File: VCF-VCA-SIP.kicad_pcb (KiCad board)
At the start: 2 copper layers, 46 x 18 mm, 45 parts, among them P1 CONN_10, Q1 BC857BS, U1 LM13700, U2 TL072-, U3 LM13700, U4 TL072-, U5 LM13700, U6 TL072-

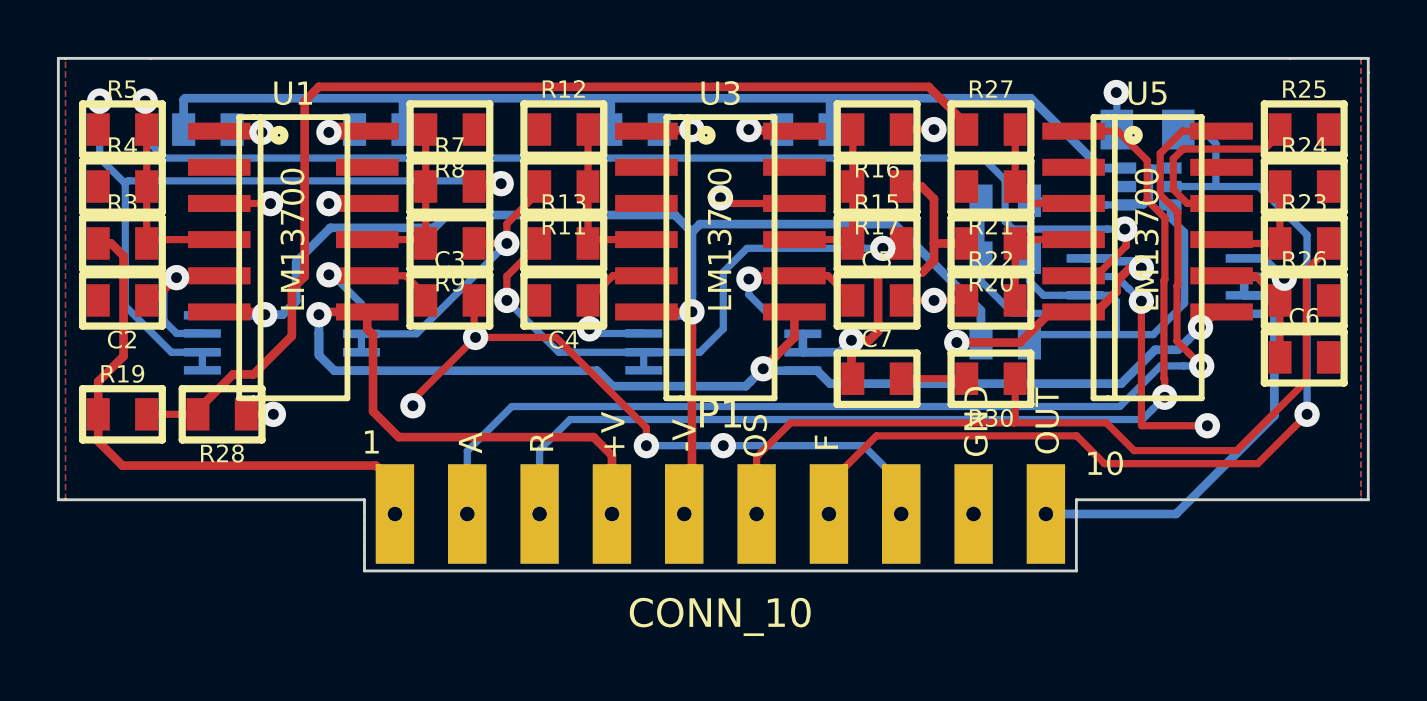
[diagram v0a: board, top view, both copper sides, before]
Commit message: done routing and arranging silkscreen references. Going to try 3D rendering next
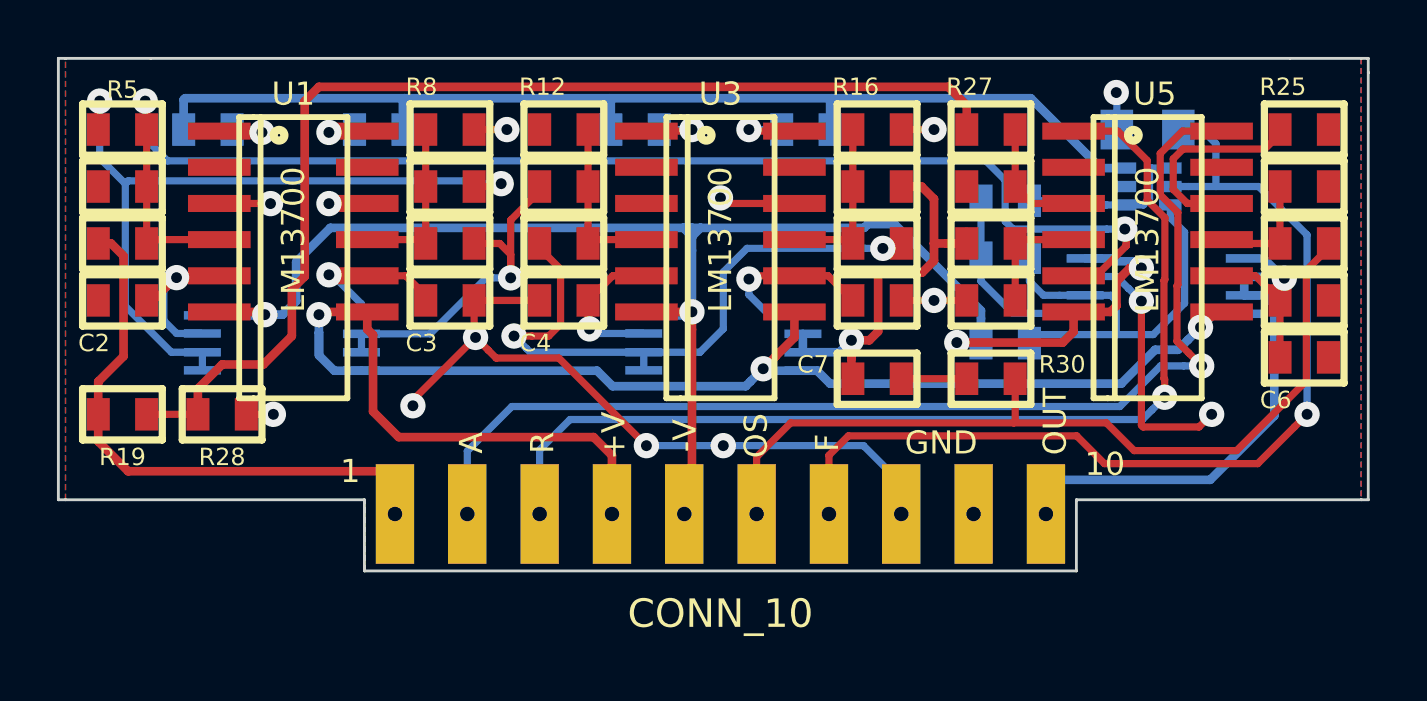
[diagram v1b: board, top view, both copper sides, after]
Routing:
- net GND: track 43.7 -> 47.1 mm, vias 13 -> 14
- net Net-(R11-Pad2): track 10.7 -> 12.6 mm
- net Net-(R13-Pad1): track 20.6 -> 22.3 mm
- net -VCC: track 58.1 -> 59.4 mm
- net Net-(R19-Pad2): track 38.9 -> 39.8 mm
- net VCF_CTRL: track 34.5 -> 35.1 mm
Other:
- board text added: "v1.1 11 2015"
- board text removed: "v1.0 11 2014"

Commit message: gerbers generated, boards ordered from dirtypcbs.com
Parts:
- moved R28 3.50 mm to (97.0, 95.5), turned to 0 degrees
- moved R19 2.00 mm to (97.0, 93.5)
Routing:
- net GND: track 47.1 -> 50.7 mm
- net Net-(R19-Pad2): track 39.8 -> 40.4 mm
